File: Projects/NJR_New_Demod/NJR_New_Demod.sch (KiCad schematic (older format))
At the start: 27 parts, among them J1 SMA-J-P-H-ST-EM1, U1 SFECF10M7EA00-R0, U2 NJM2549, U3 NJM2741

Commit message: Added a VVA
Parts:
- J_Audio1, J_Power1, J_RSSI1: footprint Connector_Phoenix_MC_HighVoltage:PhoenixContact_MCV_1,5_2-G-5.08_1x02_P5.08mm_Vertical -> Connector_PinHeader_2.54mm:PinHeader_1x02_P2.54mm_Vertical
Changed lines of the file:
@@
 F 0 "J_Audio1" H 8180 5017 50  0000 L CNN
 F 1 "Conn_01x02" H 8180 4926 50  0000 L CNN
-F 2 "Connector_Phoenix_MC_HighVoltage:PhoenixContact_MCV_1,5_2-G-5.08_1x02_P5.08mm_Vertical" H 8100 5025 50  0001 C CNN
+F 2 "Connector_PinHeader_2.54mm:PinHeader_1x02_P2.54mm_Vertical" H 8100 5025 50  0001 C CNN
 F 3 "~" H 8100 5025 50  0001 C CNN
 	1    8100 5025
@@
 F 0 "J_RSSI1" H 8155 5417 50  0000 L CNN
 F 1 "Conn_01x02" H 8155 5326 50  0000 L CNN
-F 2 "Connector_Phoenix_MC_HighVoltage:PhoenixContact_MCV_1,5_2-G-5.08_1x02_P5.08mm_Vertical" H 8075 5425 50  0001 C CNN
+F 2 "Connector_PinHeader_2.54mm:PinHeader_1x02_P2.54mm_Vertical" H 8075 5425 50  0001 C CNN
 F 3 "~" H 8075 5425 50  0001 C CNN
 	1    8075 5425
@@
 F 0 "J_Power1" H 8155 5867 50  0000 L CNN
 F 1 "Conn_01x02" H 8155 5776 50  0000 L CNN
-F 2 "Connector_Phoenix_MC_HighVoltage:PhoenixContact_MCV_1,5_2-G-5.08_1x02_P5.08mm_Vertical" H 8075 5875 50  0001 C CNN
+F 2 "Connector_PinHeader_2.54mm:PinHeader_1x02_P2.54mm_Vertical" H 8075 5875 50  0001 C CNN
 F 3 "~" H 8075 5875 50  0001 C CNN
 	1    8075 5875

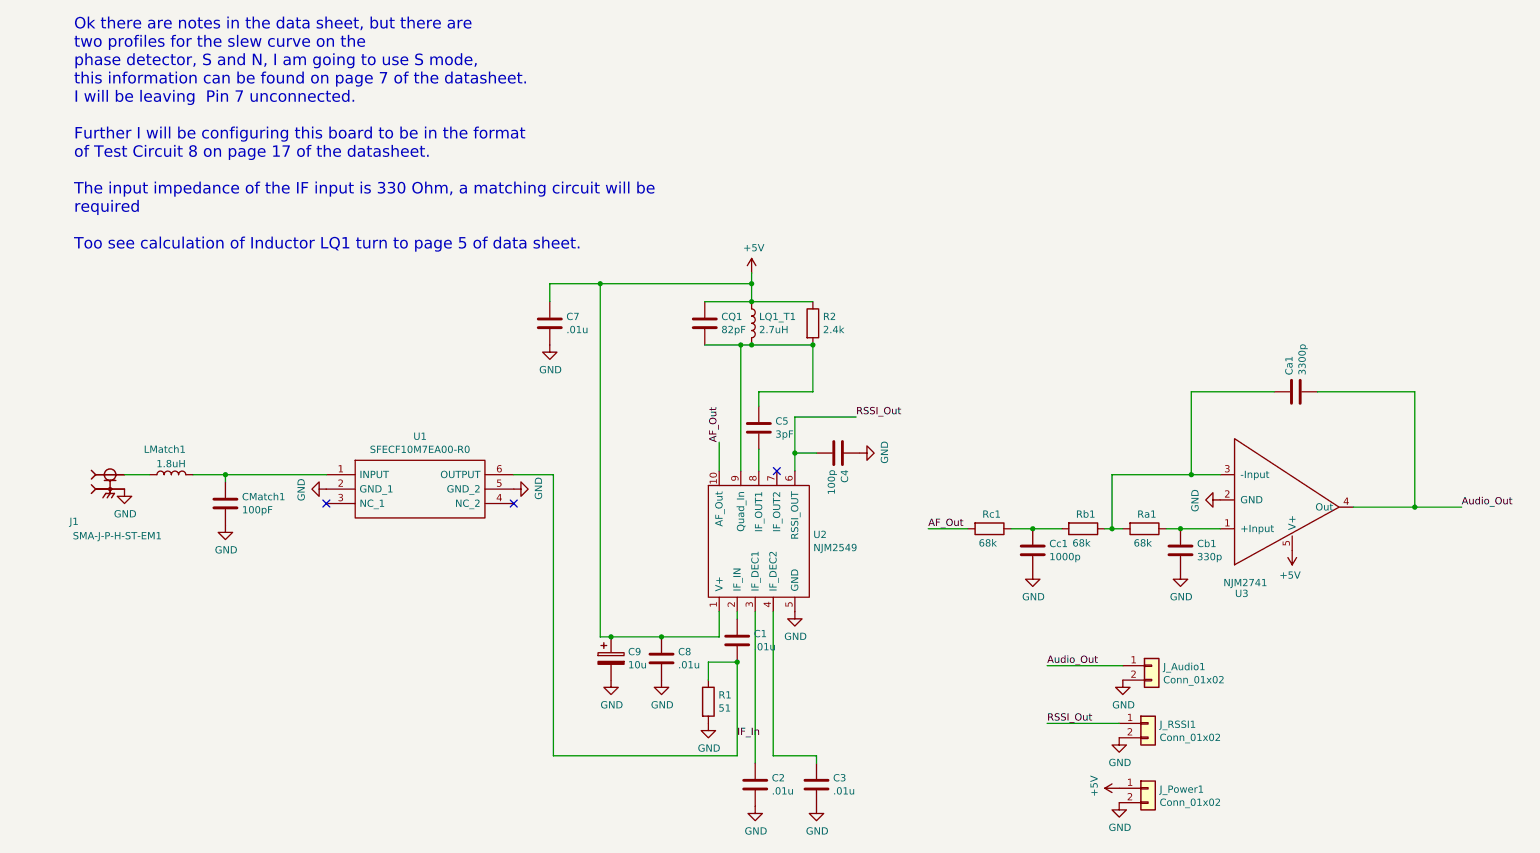
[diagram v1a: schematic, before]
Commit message: Power Detector and power splitter boards designed
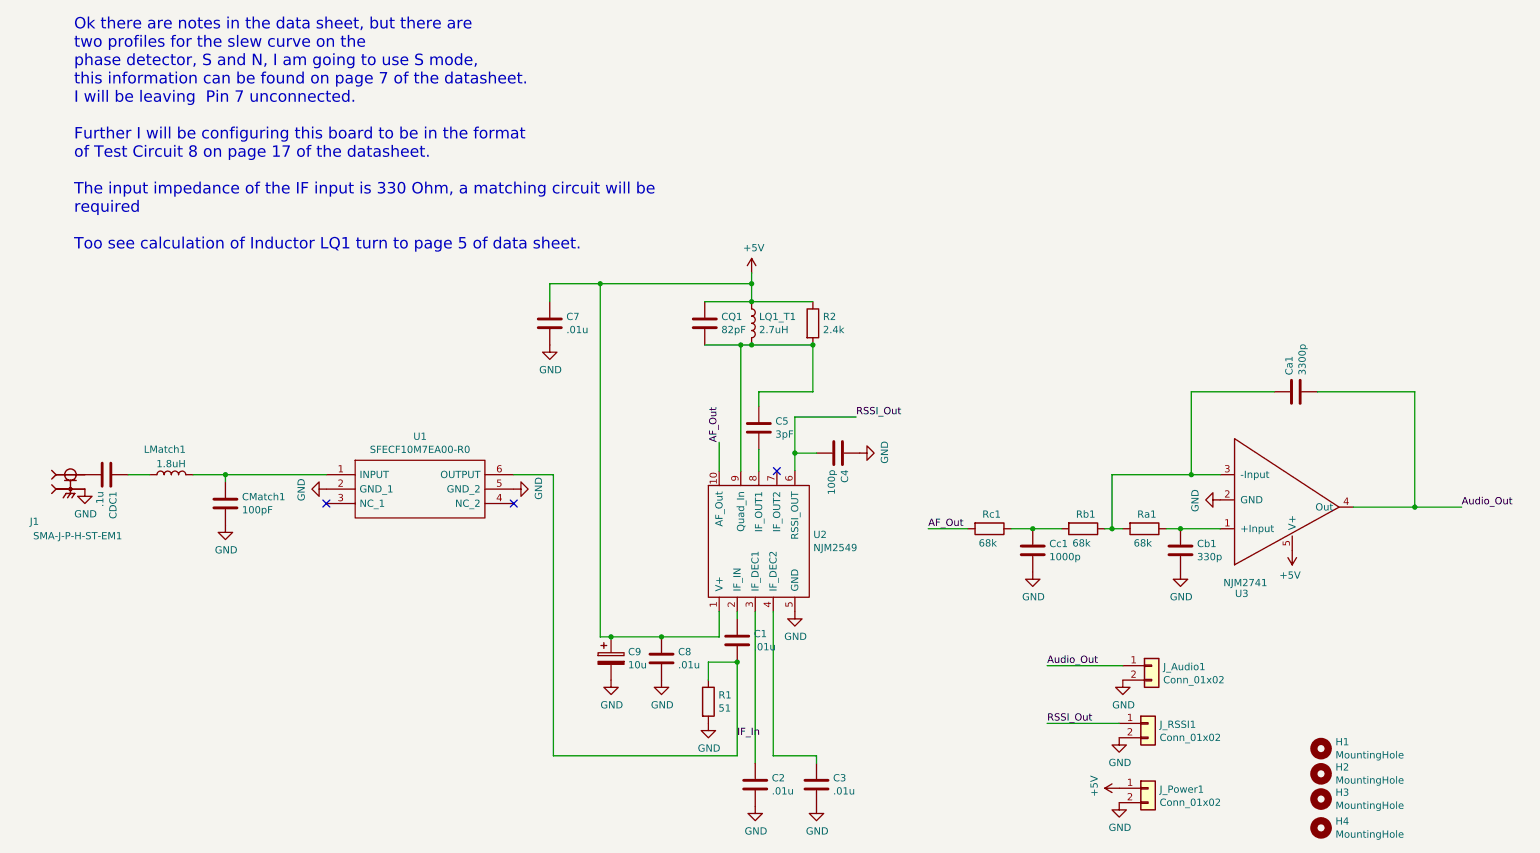
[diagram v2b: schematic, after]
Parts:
- added CDC1: .1u, Capacitor_SMD:C_0805_2012Metric, symbol Device:C
- added H1, H2, H3, H4: MountingHole, MountingHole:MountingHole_2.2mm_M2, symbol Mechanical:MountingHole
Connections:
- net at LMatch1.1: now also CDC1.1; no longer J1.1
- new net: CDC1.2, J1.1
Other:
- moved on the sheet: J1
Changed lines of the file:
@@
 	1675 3700 2375 3700
 Wire Wire Line
-	1150 3700 975  3700
+	1150 3700 1000 3700
 $Comp
 L RandomSMAIFoundOnline:SMA-J-P-H-ST-EM1 J1
 U 1 1 604D708B
-P 875 3800
-F 0 "J1" H 625 3575 50  0000 C CNN
-F 1 "SMA-J-P-H-ST-EM1" H 925 3475 50  0000 C CNN
-F 2 "SAMTEC_SMA-J-P-H-ST-EM1" H 875 3800 50  0001 L BNN
-F 3 "" H 875 3800 50  0001 L BNN
-F 4 "Samtec" H 875 3800 50  0001 L BNN "MANUFACTURER"
-F 5 "G" H 875 3800 50  0001 L BNN "PARTREV"
-F 6 "Manufacturer Recommendations" H 875 3800 50  0001 L BNN "STANDARD"
-F 7 "3.675mm" H 875 3800 50  0001 L BNN "MAXIMUM_PACKAGE_HEIGHT"
-	1    875  3800
+P 600 3800
+F 0 "J1" H 350 3575 50  0000 C CNN
+F 1 "SMA-J-P-H-ST-EM1" H 650 3475 50  0000 C CNN
+F 2 "SAMTEC_SMA-J-P-H-ST-EM1" H 600 3800 50  0001 L BNN
+F 3 "" H 600 3800 50  0001 L BNN
+F 4 "Samtec" H 600 3800 50  0001 L BNN "MANUFACTURER"
+F 5 "G" H 600 3800 50  0001 L BNN "PARTREV"
+F 6 "Manufacturer Recommendations" H 600 3800 50  0001 L BNN "STANDARD"
+F 7 "3.675mm" H 600 3800 50  0001 L BNN "MAXIMUM_PACKAGE_HEIGHT"
+	1    600  3800
 	1    0    0    -1
 $EndComp
@@
 L power:GND #PWR0117
 U 1 1 604D8615
-P 975 3800
-F 0 "#PWR0117" H 975 3550 50  0001 C CNN
-F 1 "GND" H 980 3627 50  0000 C CNN
-F 2 "" H 975 3800 50  0001 C CNN
-F 3 "" H 975 3800 50  0001 C CNN
-	1    975  3800
+P 700 3800
+F 0 "#PWR0117" H 700 3550 50  0001 C CNN
+F 1 "GND" H 705 3627 50  0000 C CNN
+F 2 "" H 700 3800 50  0001 C CNN
+F 3 "" H 700 3800 50  0001 C CNN
+	1    700  3800
 	1    0    0    -1
 $EndComp
@@
 	1    0    0    -1
 $EndComp
+$Comp
+L Device:C CDC1
+U 1 1 6054382C
+P 850 3700
+F 0 "CDC1" H 965 3746 50  0000 L CNN
+F 1 ".1u" H 965 3655 50  0000 L CNN
+F 2 "Capacitor_SMD:C_0805_2012Metric" H 888 3550 50  0001 C CNN
+F 3 "~" H 850 3700 50  0001 C CNN
+	1    850  3700
+	0    1    1    0
+$EndComp
+$Comp
+L Mechanical:MountingHole H1
+U 1 1 6056288D
+P 9275 5600
+F 0 "H1" H 9375 5646 50  0000 L CNN
+F 1 "MountingHole" H 9375 5555 50  0000 L CNN
+F 2 "MountingHole:MountingHole_2.2mm_M2" H 9275 5600 50  0001 C CNN
+F 3 "~" H 9275 5600 50  0001 C CNN
+	1    9275 5600
+	1    0    0    -1
+$EndComp
+$Comp
+L Mechanical:MountingHole H2
+U 1 1 60563DC1
+P 9275 5775
+F 0 "H2" H 9375 5821 50  0000 L CNN
+F 1 "MountingHole" H 9375 5730 50  0000 L CNN
+F 2 "MountingHole:MountingHole_2.2mm_M2" H 9275 5775 50  0001 C CNN
+F 3 "~" H 9275 5775 50  0001 C CNN
+	1    9275 5775
+	1    0    0    -1
+$EndComp
+$Comp
+L Mechanical:MountingHole H3
+U 1 1 6056400A
+P 9275 5950
+F 0 "H3" H 9375 5996 50  0000 L CNN
+F 1 "MountingHole" H 9375 5905 50  0000 L CNN
+F 2 "MountingHole:MountingHole_2.2mm_M2" H 9275 5950 50  0001 C CNN
+F 3 "~" H 9275 5950 50  0001 C CNN
+	1    9275 5950
+	1    0    0    -1
+$EndComp
+$Comp
+L Mechanical:MountingHole H4
+U 1 1 605641B5
+P 9275 6150
+F 0 "H4" H 9375 6196 50  0000 L CNN
+F 1 "MountingHole" H 9375 6105 50  0000 L CNN
+F 2 "MountingHole:MountingHole_2.2mm_M2" H 9275 6150 50  0001 C CNN
+F 3 "~" H 9275 6150 50  0001 C CNN
+	1    9275 6150
+	1    0    0    -1
+$EndComp
